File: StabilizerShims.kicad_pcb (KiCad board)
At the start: 2 copper layers, 105 x 103 mm, 42 parts

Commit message: V2
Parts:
- removed G***: LOGO, locallib:ai-ring-6mm-FancyAss-Mask
- removed G***: LOGO, locallib:ai-ring-6mm-FancyAss
- removed G***: LOGO, locallib:PolarisSmall
- removed G***: LOGO, locallib:PolarisLogo
- removed the REF** at (202.5, 138.2)
- removed the REF** at (154.0, 81.5)
- removed the REF** at (167.0, 82.0)
- removed the REF** at (171.0, 104.2)
- removed the REF** at (158.0, 82.0)
- removed the REF** at (158.0, 59.2)
- removed the REF** at (154.0, 58.8)
- removed the REF** at (158.0, 127.5)
- removed the REF** at (171.0, 81.5)
- removed the REF** at (171.0, 58.8)
- removed the REF** at (167.0, 127.5)
- removed the REF** at (202.5, 49.2)
- removed the REF** at (158.0, 104.8)
- removed the REF** at (154.0, 104.2)
- removed the REF** at (154.0, 127.0)
- removed the REF** at (144.0, 81.5)
- removed the REF** at (140.0, 82.0)
- removed the REF** at (140.0, 59.2)
- removed the REF** at (144.0, 58.8)
- removed the REF** at (140.0, 127.5)
- removed the REF** at (140.0, 104.8)
- removed the REF** at (144.0, 104.2)
- removed the REF** at (135.5, 140.2)
- removed the REF** at (144.0, 127.0)
- removed the REF** at (131.0, 82.0)
- removed the REF** at (131.0, 59.2)
- removed the REF** at (127.0, 58.8)
- removed the REF** at (127.0, 81.5)
- removed the REF** at (131.0, 104.8)
- removed the REF** at (127.0, 104.2)
- removed the REF** at (131.0, 127.5)
- removed the REF** at (162.5, 140.2)
- removed the REF** at (135.5, 47.2)
- removed the REF** at (162.5, 47.2)
- removed the REF** at (167.0, 59.2)
- removed the REF** at (167.0, 104.8)
- removed the REF** at (171.0, 127.0)
- added REF**: StabilizerShim-Holes, locallib:StabilizerShim-Holes, F.Cu at (214.5, 85.2)
- added REF**: StabilizerShim-Holes, locallib:StabilizerShim-Holes, F.Cu at (198.5, 64.5)
- added REF**: StabilizerShim-Holes, locallib:StabilizerShim-Holes, F.Cu at (198.5, 106.0)
- added REF**: StabilizerShim-Holes, locallib:StabilizerShim-Holes, F.Cu at (198.5, 126.8)
- added REF**: StabilizerShim-Holes, locallib:StabilizerShim-Holes, F.Cu at (190.5, 85.2)
- added REF**: StabilizerShim-Holes, locallib:StabilizerShim-Holes, F.Cu at (190.5, 64.5)
- added REF**: StabilizerShim-Holes, locallib:StabilizerShim-Holes, F.Cu at (190.5, 106.0)
- added REF**: StabilizerShim-Holes, locallib:StabilizerShim-Holes, F.Cu at (190.5, 126.8)
- added REF**: StabilizerShim-Holes, locallib:StabilizerShim-Holes, F.Cu at (182.5, 85.2)
- added REF**: StabilizerShim-Holes, locallib:StabilizerShim-Holes, F.Cu at (182.5, 64.5)
- added REF**: StabilizerShim-Holes, locallib:StabilizerShim-Holes, F.Cu at (182.5, 106.0)
- added REF**: StabilizerShim-Holes, locallib:StabilizerShim-Holes, F.Cu at (214.5, 64.5)
- added REF**: StabilizerShim-Holes, locallib:StabilizerShim-Holes, F.Cu at (182.5, 126.8)
- added REF**: StabilizerShim-Holes, locallib:StabilizerShim-Holes, F.Cu at (174.5, 85.2)
- added REF**: StabilizerShim-Holes, locallib:StabilizerShim-Holes, F.Cu at (174.5, 64.5)
- added REF**: StabilizerShim-Holes, locallib:StabilizerShim-Holes, F.Cu at (174.5, 106.0)
- added REF**: StabilizerShim-Holes, locallib:StabilizerShim-Holes, F.Cu at (174.5, 126.8)
- added REF**: StabilizerShim-Holes, locallib:StabilizerShim-Holes, F.Cu at (166.5, 85.2)
- added REF**: StabilizerShim-Holes, locallib:StabilizerShim-Holes, F.Cu at (166.5, 64.5)
- added REF**: StabilizerShim-Holes, locallib:StabilizerShim-Holes, F.Cu at (166.5, 106.0)
- added REF**: StabilizerShim-Holes, locallib:StabilizerShim-Holes, F.Cu at (166.5, 126.8)
- added REF**: StabilizerShim-Holes, locallib:StabilizerShim-Holes, F.Cu at (158.5, 85.2)
- added REF**: StabilizerShim-Holes, locallib:StabilizerShim-Holes, F.Cu at (214.5, 106.0)
- added REF**: StabilizerShim-Holes, locallib:StabilizerShim-Holes, F.Cu at (158.5, 64.5)
- added REF**: StabilizerShim-Holes, locallib:StabilizerShim-Holes, F.Cu at (158.5, 106.0)
- added REF**: StabilizerShim-Holes, locallib:StabilizerShim-Holes, F.Cu at (158.5, 126.8)
- added REF**: StabilizerShim-Holes, locallib:StabilizerShim-Holes, F.Cu at (150.5, 85.2)
- added REF**: StabilizerShim-Holes, locallib:StabilizerShim-Holes, F.Cu at (150.5, 64.5)
- added REF**: StabilizerShim-Holes, locallib:StabilizerShim-Holes, F.Cu at (150.5, 106.0)
- added REF**: StabilizerShim-Holes, locallib:StabilizerShim-Holes, F.Cu at (150.5, 126.8)
- added REF**: StabilizerShim-Holes, locallib:StabilizerShim-Holes, F.Cu at (142.5, 85.2)
- added REF**: StabilizerShim-Holes, locallib:StabilizerShim-Holes, F.Cu at (142.5, 64.5)
- added REF**: StabilizerShim-Holes, locallib:StabilizerShim-Holes, F.Cu at (142.5, 106.0)
- added REF**: StabilizerShim-Holes, locallib:StabilizerShim-Holes, F.Cu at (214.5, 126.8)
- added REF**: StabilizerShim-Holes, locallib:StabilizerShim-Holes, F.Cu at (142.5, 126.8)
- added REF**: StabilizerShim-Holes, locallib:StabilizerShim-Holes, F.Cu at (134.5, 85.2)
- added REF**: StabilizerShim-Holes, locallib:StabilizerShim-Holes, F.Cu at (134.5, 64.5)
- added REF**: StabilizerShim-Holes, locallib:StabilizerShim-Holes, F.Cu at (134.5, 106.0)
- added REF**: StabilizerShim-Holes, locallib:StabilizerShim-Holes, F.Cu at (134.5, 126.8)
- added REF**: StabilizerShim-Holes, locallib:StabilizerShim-Holes, F.Cu at (126.5, 64.5)
- added REF**: StabilizerShim-Holes, locallib:StabilizerShim-Holes, F.Cu at (126.5, 85.2)
- added REF**: StabilizerShim-Holes, locallib:StabilizerShim-Holes, F.Cu at (126.5, 106.0)
- added REF**: StabilizerShim-Holes, locallib:StabilizerShim-Holes, F.Cu at (206.5, 85.2)
- added REF**: StabilizerShim-Holes, locallib:StabilizerShim-Holes, F.Cu at (206.5, 64.5)
- added REF**: StabilizerShim-Holes, locallib:StabilizerShim-Holes, F.Cu at (206.5, 106.0)
- added REF**: StabilizerShim-Holes, locallib:StabilizerShim-Holes, F.Cu at (206.5, 126.8)
- added REF**: StabilizerShim-Holes, locallib:StabilizerShim-Holes, F.Cu at (198.5, 85.2)
- moved REF** 0.56 mm to (126.5, 126.8)
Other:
- board size 105 x 103 mm -> 96 x 83 mm
- board text added: "V-CUT"
- board text removed: "Assembled by"
- board text removed: "Plate:"
- board text removed: "Stabilizers:"
- board text removed: "Switches:"
- board text removed: "by Kevinplus and ai03 Distributed by KBDfans"
- board text removed: "deskeys.io kb.ai03.me kbdfans.com"

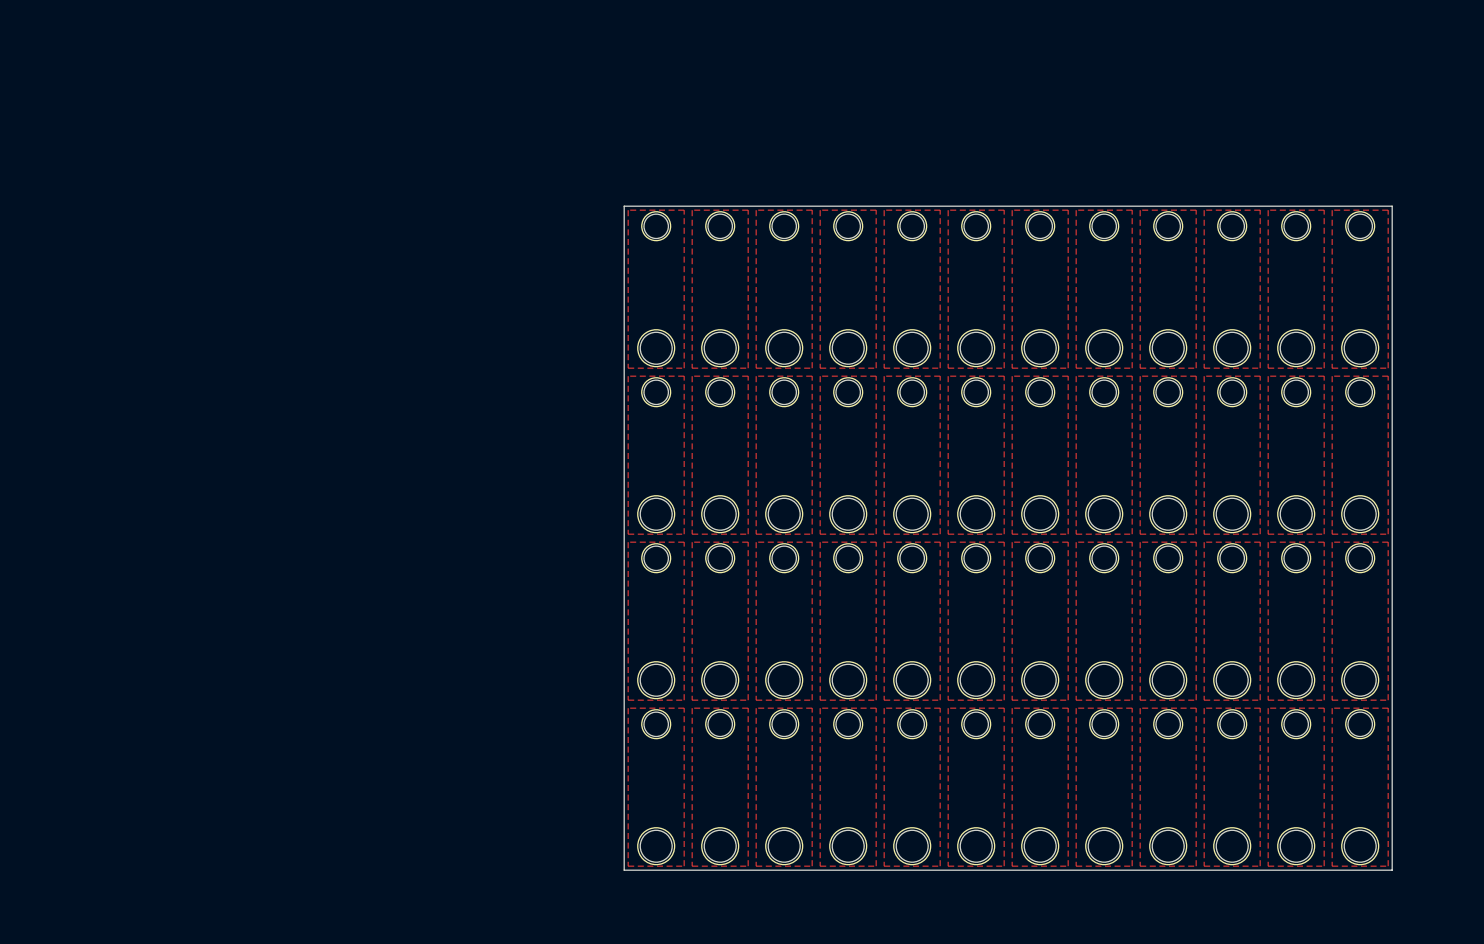
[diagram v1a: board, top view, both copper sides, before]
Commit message: Begin work on v2 shim
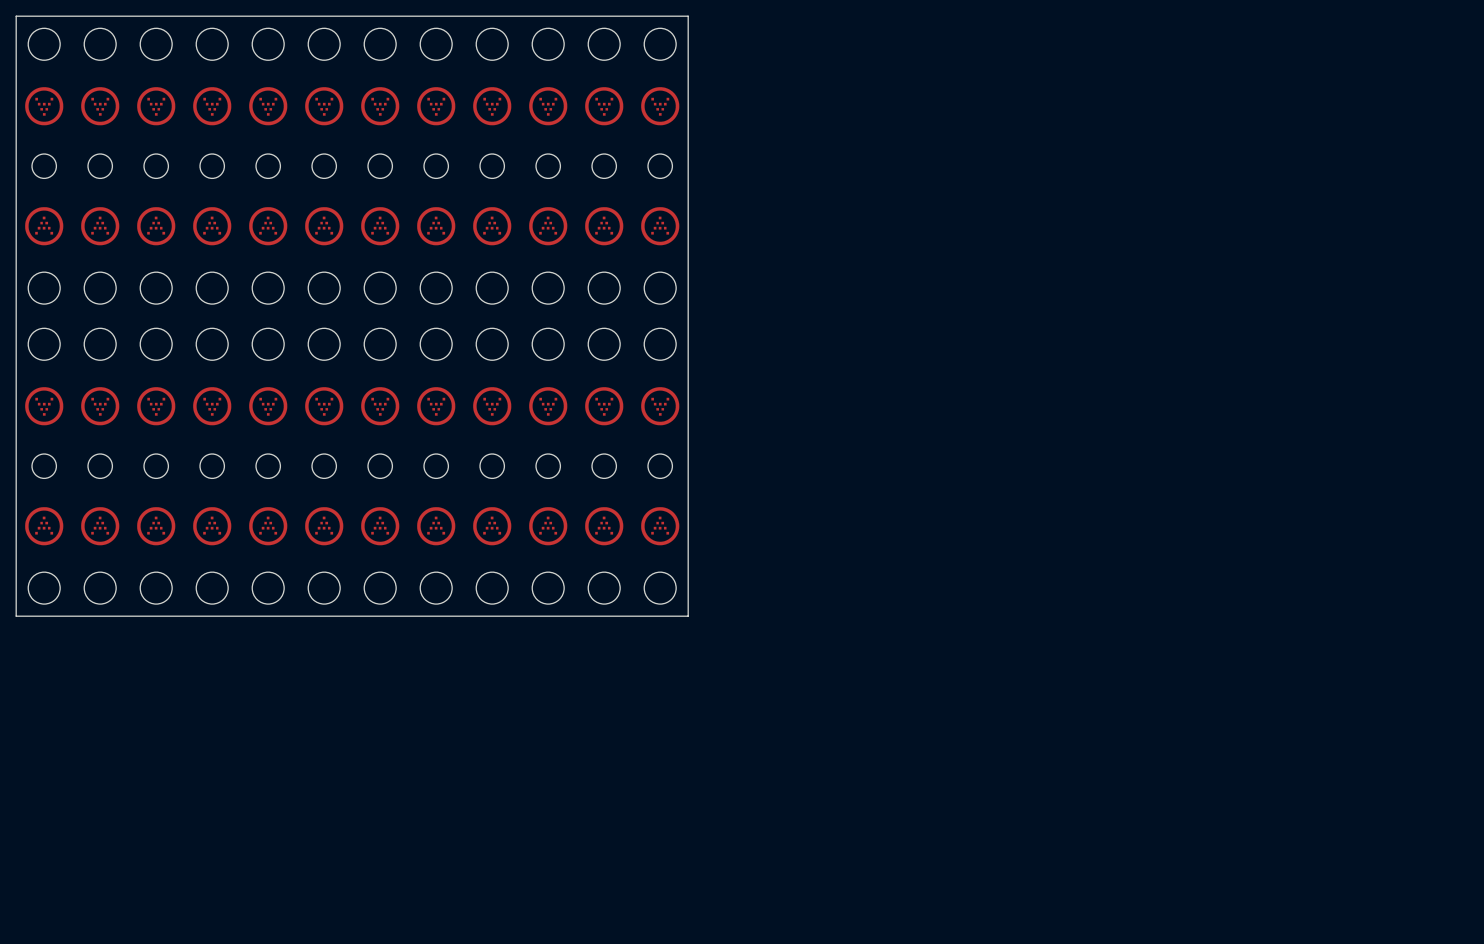
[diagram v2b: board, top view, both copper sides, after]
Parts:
- removed the REF** at (214.5, 85.2)
- removed the REF** at (198.5, 64.5)
- removed the REF** at (198.5, 106.0)
- removed the REF** at (198.5, 126.8)
- removed the REF** at (190.5, 85.2)
- removed the REF** at (190.5, 64.5)
- removed the REF** at (190.5, 106.0)
- removed the REF** at (190.5, 126.8)
- removed the REF** at (182.5, 85.2)
- removed the REF** at (182.5, 64.5)
- removed the REF** at (182.5, 106.0)
- removed the REF** at (214.5, 64.5)
- removed the REF** at (182.5, 126.8)
- removed the REF** at (174.5, 85.2)
- removed the REF** at (174.5, 64.5)
- removed the REF** at (174.5, 106.0)
- removed the REF** at (174.5, 126.8)
- removed the REF** at (166.5, 85.2)
- removed the REF** at (166.5, 64.5)
- removed the REF** at (166.5, 106.0)
- removed the REF** at (166.5, 126.8)
- removed the REF** at (158.5, 85.2)
- removed the REF** at (214.5, 106.0)
- removed the REF** at (158.5, 64.5)
- removed the REF** at (158.5, 106.0)
- removed the REF** at (158.5, 126.8)
- removed the REF** at (150.5, 85.2)
- removed the REF** at (150.5, 64.5)
- removed the REF** at (150.5, 106.0)
- removed the REF** at (150.5, 126.8)
- removed the REF** at (142.5, 85.2)
- removed the REF** at (142.5, 64.5)
- removed the REF** at (142.5, 106.0)
- removed the REF** at (214.5, 126.8)
- removed the REF** at (142.5, 126.8)
- removed the REF** at (134.5, 85.2)
- removed the REF** at (134.5, 64.5)
- removed the REF** at (134.5, 106.0)
- removed the REF** at (134.5, 126.8)
- removed the REF** at (126.5, 64.5)
- removed the REF** at (126.5, 85.2)
- removed the REF** at (126.5, 106.0)
- removed the REF** at (126.5, 126.8)
- removed the REF** at (206.5, 85.2)
- removed the REF** at (206.5, 64.5)
- removed the REF** at (206.5, 106.0)
- removed the REF** at (206.5, 126.8)
- removed the REF** at (198.5, 85.2)
- added G***: LOGO, locallib:ai-4.8-combined, F.Cu at (127.0, 95.0)
- added G***: LOGO, locallib:ai-4.8-combined, F.Cu at (64.0, 95.0)
- added G***: LOGO, locallib:ai-4.8-combined, F.Cu at (71.0, 95.0)
- added G***: LOGO, locallib:ai-4.8-combined, F.Cu at (92.0, 95.0)
- added G***: LOGO, locallib:ai-4.8-combined, F.Cu at (50.0, 80.0)
- added G***: LOGO, locallib:ai-4.8-combined, F.Cu at (120.0, 80.0)
- added G***: LOGO, locallib:ai-4.8-combined, F.Cu at (99.0, 80.0)
- added G***: LOGO, locallib:ai-4.8-combined, F.Cu at (64.0, 80.0)
- added G***: LOGO, locallib:ai-4.8-combined, F.Cu at (57.0, 80.0)
- added G***: LOGO, locallib:ai-4.8-combined, F.Cu at (127.0, 80.0)
- added G***: LOGO, locallib:ai-4.8-combined, F.Cu at (92.0, 80.0)
- added G***: LOGO, locallib:ai-4.8-combined, F.Cu at (57.0, 95.0)
- added G***: LOGO, locallib:ai-4.8-combined, F.Cu at (78.0, 80.0)
- added G***: LOGO, locallib:ai-4.8-combined, F.Cu at (71.0, 80.0)
- added G***: LOGO, locallib:ai-4.8-combined, F.Cu at (113.0, 80.0)
- added G***: LOGO, locallib:ai-4.8-combined, F.Cu at (106.0, 80.0)
- added G***: LOGO, locallib:ai-4.8-combined, F.Cu at (85.0, 80.0)
- added G***: LOGO, locallib:ai-4.8-combined, F.Cu at (127.0, 57.5)
- added G***: LOGO, locallib:ai-4.8-combined, F.Cu at (57.0, 57.5)
- added G***: LOGO, locallib:ai-4.8-combined, F.Cu at (78.0, 57.5)
- added G***: LOGO, locallib:ai-4.8-combined, F.Cu at (113.0, 57.5)
- added G***: LOGO, locallib:ai-4.8-combined, F.Cu at (120.0, 57.5)
- added G***: LOGO, locallib:ai-4.8-combined, F.Cu at (78.0, 95.0)
- added G***: LOGO, locallib:ai-4.8-combined, F.Cu at (50.0, 57.5)
- added G***: LOGO, locallib:ai-4.8-combined, F.Cu at (85.0, 57.5)
- added G***: LOGO, locallib:ai-4.8-combined, F.Cu at (99.0, 57.5)
- added G***: LOGO, locallib:ai-4.8-combined, F.Cu at (106.0, 57.5)
- added G***: LOGO, locallib:ai-4.8-combined, F.Cu at (64.0, 57.5)
- added G***: LOGO, locallib:ai-4.8-combined, F.Cu at (71.0, 57.5)
- added G***: LOGO, locallib:ai-4.8-combined, F.Cu at (92.0, 57.5)
- added G***: LOGO, locallib:ai-4.8-combined, F.Cu at (127.0, 42.5)
- added G***: LOGO, locallib:ai-4.8-combined, F.Cu at (120.0, 42.5)
- added G***: LOGO, locallib:ai-4.8-combined, F.Cu at (113.0, 42.5)
- added G***: LOGO, locallib:ai-4.8-combined, F.Cu at (113.0, 95.0)
- added G***: LOGO, locallib:ai-4.8-combined, F.Cu at (106.0, 42.5)
- added G***: LOGO, locallib:ai-4.8-combined, F.Cu at (99.0, 42.5)
- added G***: LOGO, locallib:ai-4.8-combined, F.Cu at (92.0, 42.5)
- added G***: LOGO, locallib:ai-4.8-combined, F.Cu at (85.0, 42.5)
- added G***: LOGO, locallib:ai-4.8-combined, F.Cu at (78.0, 42.5)
- added G***: LOGO, locallib:ai-4.8-combined, F.Cu at (71.0, 42.5)
- added G***: LOGO, locallib:ai-4.8-combined, F.Cu at (64.0, 42.5)
- added G***: LOGO, locallib:ai-4.8-combined, F.Cu at (57.0, 42.5)
- added G***: LOGO, locallib:ai-4.8-combined, F.Cu at (50.0, 42.5)
- added G***: LOGO, locallib:ai-4.8-combined, F.Cu at (120.0, 95.0)
- added G***: LOGO, locallib:ai-4.8-combined, F.Cu at (50.0, 95.0)
- added G***: LOGO, locallib:ai-4.8-combined, F.Cu at (85.0, 95.0)
- added G***: LOGO, locallib:ai-4.8-combined, F.Cu at (99.0, 95.0)
- added G***: LOGO, locallib:ai-4.8-combined, F.Cu at (106.0, 95.0)
- added REF**: StabilizerShim-Holes, locallib:StabilizerShim-Holes, F.Cu at (127.0, 87.5)
- added REF**: StabilizerShim-Holes, locallib:StabilizerShim-Holes, F.Cu at (120.0, 87.5)
- added REF**: StabilizerShim-Holes, locallib:StabilizerShim-Holes, F.Cu at (106.0, 87.5)
- added REF**: StabilizerShim-Holes, locallib:StabilizerShim-Holes, F.Cu at (50.0, 87.5)
- added REF**: StabilizerShim-Holes, locallib:StabilizerShim-Holes, F.Cu at (127.0, 50.0)
- added REF**: StabilizerShim-Holes, locallib:StabilizerShim-Holes, F.Cu at (120.0, 50.0)
- added REF**: StabilizerShim-Holes, locallib:StabilizerShim-Holes, F.Cu at (113.0, 50.0)
- added REF**: StabilizerShim-Holes, locallib:StabilizerShim-Holes, F.Cu at (106.0, 50.0)
- added REF**: StabilizerShim-Holes, locallib:StabilizerShim-Holes, F.Cu at (99.0, 50.0)
- added REF**: StabilizerShim-Holes, locallib:StabilizerShim-Holes, F.Cu at (92.0, 50.0)
- added REF**: StabilizerShim-Holes, locallib:StabilizerShim-Holes, F.Cu at (85.0, 50.0)
- added REF**: StabilizerShim-Holes, locallib:StabilizerShim-Holes, F.Cu at (113.0, 87.5)
- added REF**: StabilizerShim-Holes, locallib:StabilizerShim-Holes, F.Cu at (78.0, 50.0)
- added REF**: StabilizerShim-Holes, locallib:StabilizerShim-Holes, F.Cu at (71.0, 50.0)
- added REF**: StabilizerShim-Holes, locallib:StabilizerShim-Holes, F.Cu at (64.0, 50.0)
- added REF**: StabilizerShim-Holes, locallib:StabilizerShim-Holes, F.Cu at (57.0, 50.0)
- added REF**: StabilizerShim-Holes, locallib:StabilizerShim-Holes, F.Cu at (50.0, 50.0)
- added REF**: StabilizerShim-Holes, locallib:StabilizerShim-Holes, F.Cu at (71.0, 87.5)
- added REF**: StabilizerShim-Holes, locallib:StabilizerShim-Holes, F.Cu at (57.0, 87.5)
- added REF**: StabilizerShim-Holes, locallib:StabilizerShim-Holes, F.Cu at (78.0, 87.5)
- added REF**: StabilizerShim-Holes, locallib:StabilizerShim-Holes, F.Cu at (99.0, 87.5)
- added REF**: StabilizerShim-Holes, locallib:StabilizerShim-Holes, F.Cu at (92.0, 87.5)
- added REF**: StabilizerShim-Holes, locallib:StabilizerShim-Holes, F.Cu at (85.0, 87.5)
- added REF**: StabilizerShim-Holes, locallib:StabilizerShim-Holes, F.Cu at (64.0, 87.5)
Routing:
- removed copper zone on F.Cu, net (none)
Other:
- board size 96 x 83 mm -> 84 x 75 mm
